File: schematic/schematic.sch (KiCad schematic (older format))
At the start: 12 parts, among them SW1 SW_DIP_x01, U1 Teensy3.2_outer_pins, U2 BALANCE_ALARM

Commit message: Basic robot working.
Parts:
- removed U1: Teensy3.2_outer_pins, symbol Teensy3.2_outer_pins
- added CSENSE1, CSENSE2: W4953-A-COLOR-SENSOR, symbol W4953-A-COLOR-SENSOR
- added SW2: SW_Push, symbol SW_Push
- added U1: Teensy3.5_outer_pins, symbol Teensy3.5_outer_pins
- R1: value 400k -> 470k
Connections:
- net 3V3: now also OLED1.~ (Vcc(2.8-5.5V)), CSENSE1.~ (SDA), CSENSE2.~ (SDA), U1.~ (TX5_SCL0'A14_33)
- net 5V: now also U1.~ (TX5_SCL0'A14_33); no longer OLED1.~ (Vcc(2.8-5.5V))
- net CAM_RX: now also U1.~ (TX5_SCL0'A14_33)
- net CAM_TX: now also U1.~ (TX5_SCL0'A14_33)
- net GND: now also CSENSE1.~ (SDA), CSENSE2.~ (SDA), U1.~ (TX5_SCL0'A14_33)
- net LEncoderA: now also U1.~ (TX5_SCL0'A14_33)
- net LEncoderB: now also U1.~ (TX5_SCL0'A14_33)
- net L_FWD: now also U1.~ (TX5_SCL0'A14_33)
- net L_REV: now also U1.~ (TX5_SCL0'A14_33)
- net OLED_CS: now also U1.~ (TX5_SCL0'A14_33)
- net OLED_DC: now also U1.~ (TX5_SCL0'A14_33)
- net OLED_MOSI: now also U1.~ (TX5_SCL0'A14_33)
- net OLED_RESET: now also U1.~ (TX5_SCL0'A14_33)
- net OLED_SCK: now also U1.~ (TX5_SCL0'A14_33)
- net REncoderA: now also U1.~ (TX5_SCL0'A14_33)
- net REncoderB: now also U1.~ (TX5_SCL0'A14_33)
- net R_FWD: now also U1.~ (TX5_SCL0'A14_33)
- net R_REV: now also U1.~ (TX5_SCL0'A14_33)
- net at R1.2, R2.1: now also U1.~ (TX5_SCL0'A14_33)
- new net: SW2.1, U1.~ (TX5_SCL0'A14_33)
- new net: SW2.2, U1.~ (TX5_SCL0'A14_33)
- new net SCL0: CSENSE1.~ (SDA), CSENSE2.~ (SDA), U1.~ (TX5_SCL0'A14_33)
- new net SDA0: CSENSE1.~ (SDA), CSENSE2.~ (SDA), U1.~ (TX5_SCL0'A14_33)
- no-connect marks 16 -> 8
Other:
- note removed: "<- future: gyro i2c, \n<- interrupt\n"
- note removed: "GND: Power ground\nVCC: 2.8-5.5V power supply\nD0: CLK clock\nD1: MOSI data\nRST: Reset\nDC: Data / command\nCS: Chip-select signal"
- moved on the sheet: CAM1, L_MTR1, MCC1, R_MTR1
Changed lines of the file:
@@
 encoding utf-8
 Sheet 1 1
-Title ""
+Title "Colored Line Following Robot"
 Date ""
-Rev ""
-Comp ""
-Comment1 ""
-Comment2 ""
-Comment3 ""
+Rev "0"
+Comp "Brian Erickson"
+Comment1 "comment 1"
+Comment2 "comment 2"
+Comment3 "comment 3"
 Comment4 ""
 $EndDescr
-Text GLabel 7000 4250 0    60   Input ~ 0
+Text GLabel 6250 4500 0    60   Input ~ 0
 LMotor-
-Text GLabel 7000 4750 0    60   Input ~ 0
+Text GLabel 6250 5000 0    60   Input ~ 0
 LMotor+
-Text GLabel 7000 4350 0    60   Input ~ 0
-GND
-Text GLabel 7000 4450 0    60   Input ~ 0
-3V3
-Text GLabel 7000 4550 0    60   Input ~ 0
+Text GLabel 6250 4600 0    60   Input ~ 0
+GND
+Text GLabel 6250 4700 0    60   Input ~ 0
+3V3
+Text GLabel 6250 4800 0    60   Input ~ 0
 LEncoderA
-Text GLabel 7000 4650 0    60   Input ~ 0
+Text GLabel 6250 4900 0    60   Input ~ 0
 LEncoderB
-Text GLabel 8650 4250 0    60   Input ~ 0
+Text GLabel 7900 4500 0    60   Input ~ 0
 RMotor-
-Text GLabel 8650 4750 0    60   Input ~ 0
+Text GLabel 7900 5000 0    60   Input ~ 0
 LMotor+
-Text GLabel 8650 4350 0    60   Input ~ 0
-GND
-Text GLabel 8650 4450 0    60   Input ~ 0
-3V3
-Text GLabel 8650 4550 0    60   Input ~ 0
+Text GLabel 7900 4600 0    60   Input ~ 0
+GND
+Text GLabel 7900 4700 0    60   Input ~ 0
+3V3
+Text GLabel 7900 4800 0    60   Input ~ 0
 REncoderA
-Text GLabel 8650 4650 0    60   Input ~ 0
+Text GLabel 7900 4900 0    60   Input ~ 0
 REncoderB
 Text GLabel 2500 6100 1    60   Input ~ 0
 GND
 Text GLabel 2600 6100 1    60   Input ~ 0
-5V
+3V3
 Text GLabel 2700 6100 1    60   Input ~ 0
 OLED_SCK
@@
 Text GLabel 9250 3550 0    60   Input ~ 0
 BAT-
-$Comp
-L Teensy3.2_outer_pins U1
-U 1 1 5A4FD2BC
-P 4950 2300
-F 0 "U1" H 4950 3100 60  0000 C CNN
-F 1 "Teensy3.2_outer_pins" H 4950 1350 60  0000 C CNN
-F 2 "" H 4950 2300 60  0000 C CNN
-F 3 "" H 4950 2300 60  0000 C CNN
-	1    4950 2300
-	1    0    0    -1
-$EndComp
-Text GLabel 3950 1700 0    60   Input ~ 0
+Text GLabel 3300 1700 0    60   Input ~ 0
 GND
 Text GLabel 5950 1700 2    60   Input ~ 0
@@
 L ENCODER_MOTOR L_MTR1
 U 1 1 5A4FD5AE
-P 7350 4450
-F 0 "L_MTR1" H 7350 4800 60  0000 C CNN
-F 1 "ENCODER_MOTOR" H 7400 4000 60  0000 C CNN
-F 2 "" H 7300 4050 60  0001 C CNN
-F 3 "" H 7300 4050 60  0001 C CNN
-	1    7350 4450
+P 6600 4700
+F 0 "L_MTR1" H 6600 5050 60  0000 C CNN
+F 1 "ENCODER_MOTOR" H 6650 4250 60  0000 C CNN
+F 2 "" H 6550 4300 60  0001 C CNN
+F 3 "" H 6550 4300 60  0001 C CNN
+	1    6600 4700
 	1    0    0    -1
 $EndComp
@@
 L ENCODER_MOTOR R_MTR1
 U 1 1 5A4FD6E6
-P 9000 4450
-F 0 "R_MTR1" H 9000 4800 60  0000 C CNN
-F 1 "ENCODER_MOTOR" H 9050 4000 60  0000 C CNN
-F 2 "" H 8950 4050 60  0001 C CNN
-F 3 "" H 8950 4050 60  0001 C CNN
-	1    9000 4450
+P 8250 4700
+F 0 "R_MTR1" H 8250 5050 60  0000 C CNN
+F 1 "ENCODER_MOTOR" H 8300 4250 60  0000 C CNN
+F 2 "" H 8200 4300 60  0001 C CNN
+F 3 "" H 8200 4300 60  0001 C CNN
+	1    8250 4700
 	1    0    0    -1
 $EndComp
@@
 $EndComp
 Text GLabel 5950 3000 2    60   Input ~ 0
-OLED_CLK
-Text GLabel 3950 2900 0    60   Input ~ 0
+OLED_SCK
+Text GLabel 3300 2900 0    60   Input ~ 0
 OLED_MOSI
-Text GLabel 3950 2800 0    60   Input ~ 0
+Text GLabel 3300 2800 0    60   Input ~ 0
 OLED_CS
-Text GLabel 3950 2600 0    60   Input ~ 0
+Text GLabel 3300 3000 0    60   Input ~ 0
 OLED_DC
-Text GLabel 3950 2700 0    60   Input ~ 0
+Text GLabel 3300 2700 0    60   Input ~ 0
 OLED_RESET
 $Comp
 L JEVOIS CAM1
 U 1 1 5A4FDEE7
-P 2250 2100
-F 0 "CAM1" H 2250 2450 60  0000 C CNN
-F 1 "JEVOIS" H 2250 1700 60  0000 C CNN
-F 2 "" H 2100 2200 60  0001 C CNN
-F 3 "" H 2100 2200 60  0001 C CNN
-	1    2250 2100
+P 7050 6050
+F 0 "CAM1" H 7050 6400 60  0000 C CNN
+F 1 "JEVOIS" H 7050 5650 60  0000 C CNN
+F 2 "" H 6900 6150 60  0001 C CNN
+F 3 "" H 6900 6150 60  0001 C CNN
+	1    7050 6050
 	-1   0    0    -1
 $EndComp
-Text GLabel 2900 2000 2    60   Input ~ 0
-GND
-Text GLabel 2900 1900 2    60   Input ~ 0
-3V3
-Text GLabel 1600 2200 0    60   Input ~ 0
+Text GLabel 7700 5950 2    60   Input ~ 0
+GND
+Text GLabel 7700 5850 2    60   Input ~ 0
+3V3
+Text GLabel 6400 6150 0    60   Input ~ 0
 5V
-Text GLabel 1600 2300 0    60   Input ~ 0
-GND
-Text GLabel 2900 2200 2    60   Input ~ 0
+Text GLabel 6400 6250 0    60   Input ~ 0
+GND
+Text GLabel 7700 6150 2    60   Input ~ 0
 CAM_TX
-Text GLabel 2900 2100 2    60   Input ~ 0
+Text GLabel 7700 6050 2    60   Input ~ 0
 CAM_RX
-Text GLabel 3950 1800 0    60   Input ~ 0
+Text GLabel 3300 1800 0    60   Input ~ 0
 CAM_TX
-Text GLabel 3950 1900 0    60   Input ~ 0
+Text GLabel 3300 1900 0    60   Input ~ 0
 CAM_RX
 $Comp
 L MOTOR_CONTROLLER_WANGDD22 MCC1
 U 1 1 5A4FE9B8
-P 2750 3750
-F 0 "MCC1" H 2750 4300 60  0000 C CNN
-F 1 "MOTOR_CONTROLLER_WANGDD22" H 2750 3250 60  0000 C CNN
-F 2 "" H 2500 3550 60  0001 C CNN
-F 3 "" H 2500 3550 60  0001 C CNN
-	1    2750 3750
-	1    0    0    -1
-$EndComp
-Text GLabel 2100 3650 0    60   Input ~ 0
+P 4600 6200
+F 0 "MCC1" H 4600 6750 60  0000 C CNN
+F 1 "MOTOR_CONTROLLER_WANGDD22" H 4600 5700 60  0000 C CNN
+F 2 "" H 4350 6000 60  0001 C CNN
+F 3 "" H 4350 6000 60  0001 C CNN
+	1    4600 6200
+	1    0    0    -1
+$EndComp
+Text GLabel 3950 6100 0    60   Input ~ 0
 L_FWD
-Text GLabel 2100 3750 0    60   Input ~ 0
+Text GLabel 3950 6200 0    60   Input ~ 0
 L_REV
-Text GLabel 2100 3900 0    60   Input ~ 0
+Text GLabel 3950 6350 0    60   Input ~ 0
 R_FWD
-Text GLabel 2100 4000 0    60   Input ~ 0
+Text GLabel 3950 6450 0    60   Input ~ 0
 R_REV
-Text GLabel 3500 3650 2    60   Input ~ 0
+Text GLabel 5350 6100 2    60   Input ~ 0
 LMotor-
-Text GLabel 3500 3550 2    60   Input ~ 0
+Text GLabel 5350 6000 2    60   Input ~ 0
 LMotor+
-Text GLabel 3500 3900 2    60   Input ~ 0
+Text GLabel 5350 6350 2    60   Input ~ 0
 RMotor-
-Text GLabel 3500 3800 2    60   Input ~ 0
+Text GLabel 5350 6250 2    60   Input ~ 0
 LMotor+
-Text GLabel 2100 3400 0    60   Input ~ 0
+Text GLabel 3950 5850 0    60   Input ~ 0
 BAT+
-Text GLabel 2100 3500 0    60   Input ~ 0
+Text GLabel 3950 5950 0    60   Input ~ 0
 BAT-
-Text GLabel 3950 2300 0    60   Input ~ 0
+Text GLabel 3300 2300 0    60   Input ~ 0
 L_FWD
-Text GLabel 3950 2400 0    60   Input ~ 0
+Text GLabel 3300 2400 0    60   Input ~ 0
 L_REV
 Text GLabel 5950 2100 2    60   Input ~ 0
@@
 Text GLabel 5950 2200 2    60   Input ~ 0
 R_REV
-Text GLabel 5950 2600 2    60   Input ~ 0
+Text GLabel 5950 2800 2    60   Input ~ 0
 LEncoderA
-Text GLabel 5950 2700 2    60   Input ~ 0
+Text GLabel 5950 2900 2    60   Input ~ 0
 LEncoderB
-Text GLabel 5950 2800 2    60   Input ~ 0
+Text GLabel 3300 2500 0    60   Input ~ 0
 REncoderA
-Text GLabel 5950 2900 2    60   Input ~ 0
+Text GLabel 3300 2600 0    60   Input ~ 0
 REncoderB
 NoConn ~ 5950 1800
@@
 NoConn ~ 9150 1800
 NoConn ~ 9050 1800
-NoConn ~ 3950 2000
-NoConn ~ 3950 2100
-NoConn ~ 3950 2200
-NoConn ~ 3950 2500
-NoConn ~ 3950 3000
 $Comp
 L SW_DIP_x01 SW1
@@
 P 7450 1850
 F 0 "R1" V 7530 1850 50  0000 C CNN
-F 1 "400k" V 7450 1850 50  0000 C CNN
+F 1 "470k" V 7450 1850 50  0000 C CNN
 F 2 "" V 7380 1850 50  0001 C CNN
 F 3 "" H 7450 1850 50  0001 C CNN
@@
 $EndComp
 $Comp
-L GND #PWR01
+L GND #PWR1
 U 1 1 5A511792
 P 7450 2350
-F 0 "#PWR01" H 7450 2100 50  0001 C CNN
+F 0 "#PWR1" H 7450 2100 50  0001 C CNN
 F 1 "GND" H 7450 2200 50  0000 C CNN
 F 2 "" H 7450 2350 50  0001 C CNN
@@
 Connection ~ 7450 1550
 Connection ~ 7450 950
-Text Notes 6050 2450 0    60   ~ 0
-<- future: gyro i2c, \n<- interrupt\n
-NoConn ~ 5950 2400
-NoConn ~ 5950 2500
-NoConn ~ 5950 2300
-$Comp
-L PWR_FLAG #FLG02
+$Comp
+L PWR_FLAG #FLG1
 U 1 1 5A51263B
 P 7700 950
-F 0 "#FLG02" H 7700 1025 50  0001 C CNN
+F 0 "#FLG1" H 7700 1025 50  0001 C CNN
 F 1 "PWR_FLAG" H 7700 1100 50  0000 C CNN
 F 2 "" H 7700 950 50  0001 C CNN
@@
 	1    0    0    -1
 $EndComp
-Text Notes 1100 5950 0    60   ~ 0
-GND: Power ground\nVCC: 2.8-5.5V power supply\nD0: CLK clock\nD1: MOSI data\nRST: Reset\nDC: Data / command\nCS: Chip-select signal
+$Comp
+L W4953-A-COLOR-SENSOR CSENSE1
+U 1 1 5A58EBFA
+P 9300 4700
+F 0 "CSENSE1" H 9250 5050 60  0000 C CNN
+F 1 "W4953-A-COLOR-SENSOR" H 9300 4350 60  0000 C CNN
+F 2 "" H 9200 4500 60  0001 C CNN
+F 3 "" H 9200 4500 60  0001 C CNN
+	1    9300 4700
+	1    0    0    -1
+$EndComp
+$Comp
+L W4953-A-COLOR-SENSOR CSENSE2
+U 1 1 5A58EC49
+P 9300 5650
+F 0 "CSENSE2" H 9250 6000 60  0000 C CNN
+F 1 "W4953-A-COLOR-SENSOR" H 9300 5300 60  0000 C CNN
+F 2 "" H 9200 5450 60  0001 C CNN
+F 3 "" H 9200 5450 60  0001 C CNN
+	1    9300 5650
+	1    0    0    -1
+$EndComp
+Text GLabel 9000 5500 0    60   Input ~ 0
+GND
+Text GLabel 9000 5600 0    60   Input ~ 0
+3V3
+Text GLabel 9000 5700 0    60   Input ~ 0
+SCL0
+Text GLabel 9000 5800 0    60   Input ~ 0
+SDA0
+Text GLabel 5950 2400 2    60   Input ~ 0
+SCL0
+Text GLabel 5950 2500 2    60   Input ~ 0
+SDA0
+Text GLabel 9000 4550 0    60   Input ~ 0
+GND
+Text GLabel 9000 4650 0    60   Input ~ 0
+3V3
+Text GLabel 9000 4750 0    60   Input ~ 0
+SCL0
+Text GLabel 9000 4850 0    60   Input ~ 0
+SDA0
+$Comp
+L Teensy3.5_outer_pins U1
+U 1 1 5A590923
+P 4600 3050
+F 0 "U1" H 4600 4600 60  0000 C CNN
+F 1 "Teensy3.5_outer_pins" H 4600 1900 60  0000 C CNN
+F 2 "" H 4600 3800 60  0000 C CNN
+F 3 "" H 4600 3800 60  0000 C CNN
+	1    4600 3050
+	1    0    0    -1
+$EndComp
+$Comp
+L SW_Push SW2
+U 1 1 5A5D70A9
+P 2800 3800
+F 0 "SW2" H 2850 3900 50  0000 L CNN
+F 1 "SW_Push" H 2800 3740 50  0000 C CNN
+F 2 "" H 2800 4000 50  0001 C CNN
+F 3 "" H 2800 4000 50  0001 C CNN
+	1    2800 3800
+	1    0    0    -1
+$EndComp
+Wire Wire Line
+	2600 3800 2600 4000
+Wire Wire Line
+	2600 4000 3300 4000
+Wire Wire Line
+	3300 3800 3000 3800
 $EndSCHEMATC

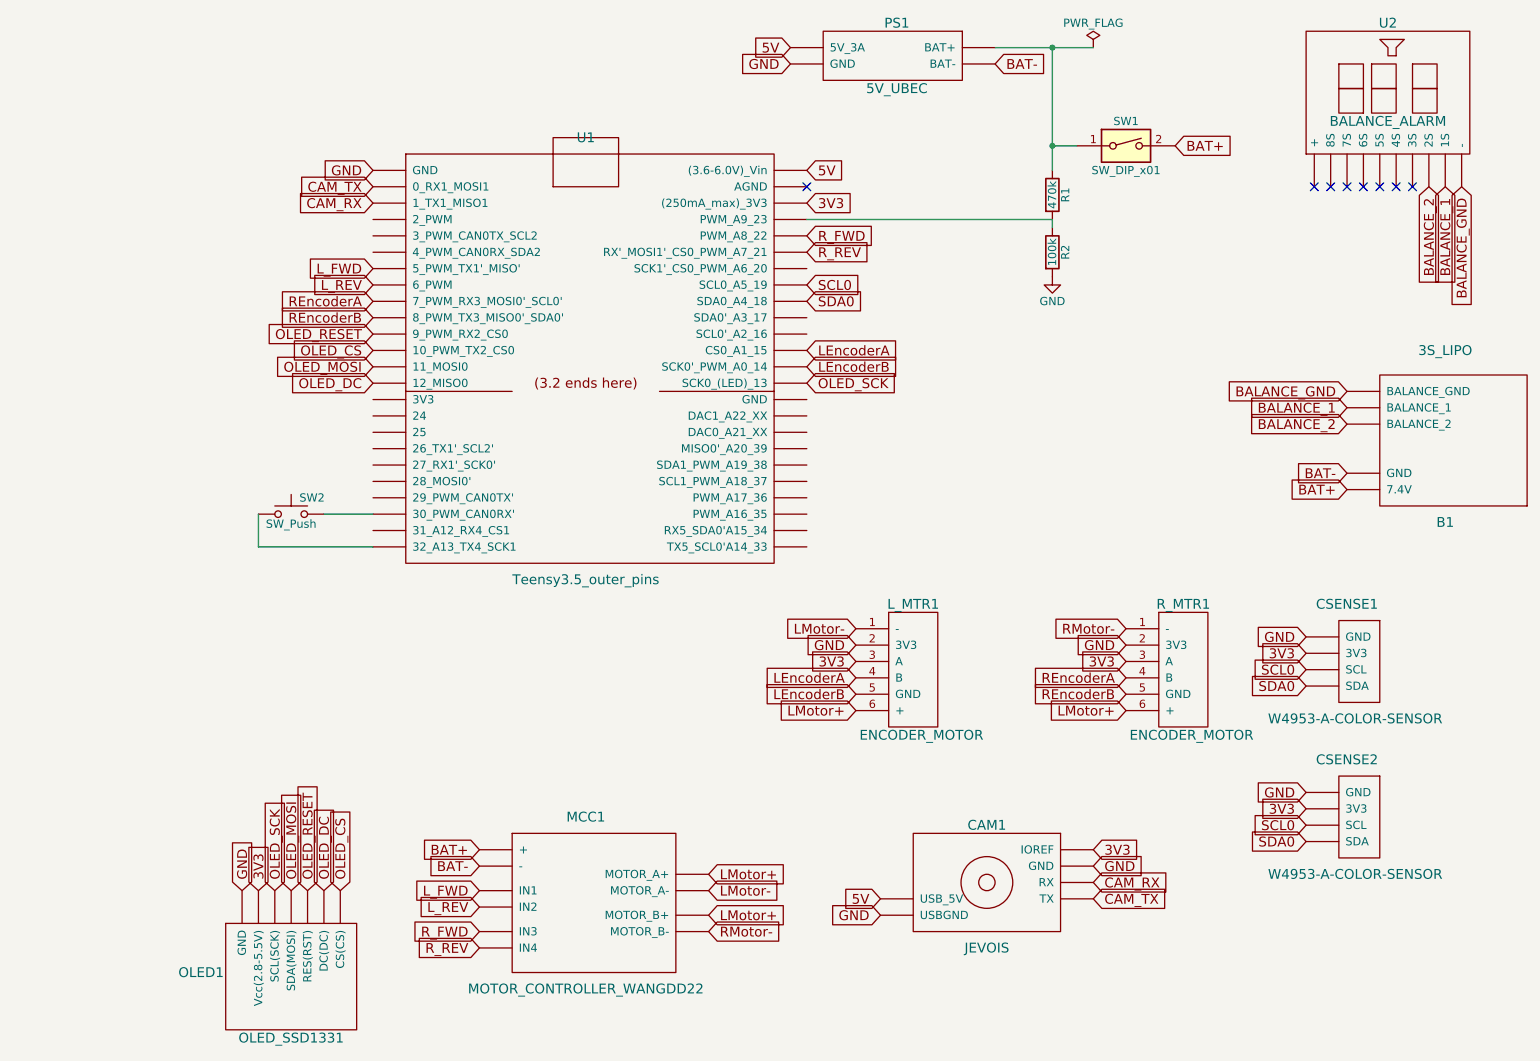
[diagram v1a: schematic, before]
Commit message: Added bluetooth, fixed motors.
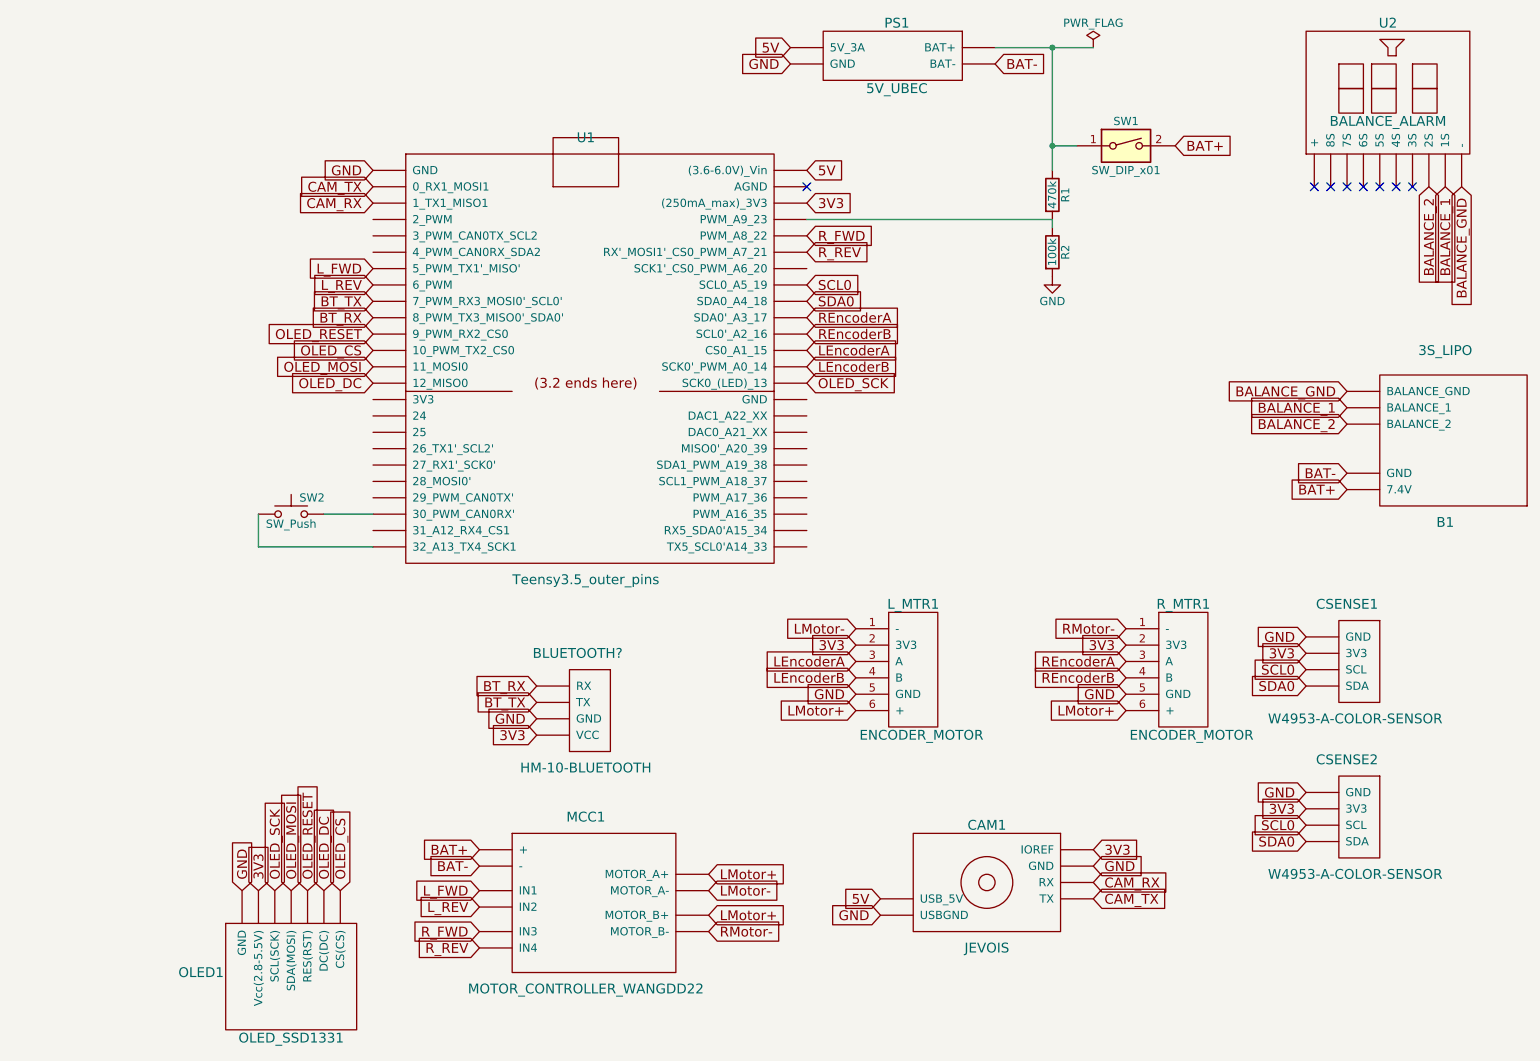
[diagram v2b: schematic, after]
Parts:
- added BLUETOOTH?: HM-10-BLUETOOTH, symbol HM-10-BLUETOOTH
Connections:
- net 3V3: now also L_MTR1.2 (3V3), R_MTR1.2 (3V3), BLUETOOTH?.~ (VCC); no longer L_MTR1.3 (A), R_MTR1.3 (A)
- net GND: now also L_MTR1.5 (GND), R_MTR1.5 (GND), BLUETOOTH?.~ (VCC); no longer L_MTR1.2 (3V3), R_MTR1.2 (3V3)
- net LEncoderA: now also L_MTR1.3 (A); no longer L_MTR1.4 (B)
- net LEncoderB: now also L_MTR1.4 (B); no longer L_MTR1.5 (GND)
- net REncoderA: now also R_MTR1.3 (A); no longer R_MTR1.4 (B)
- net REncoderB: now also R_MTR1.4 (B); no longer R_MTR1.5 (GND)
- new net BT_RX: BLUETOOTH?.~ (VCC), U1.~ (TX5_SCL0'A14_33)
- new net BT_TX: BLUETOOTH?.~ (VCC), U1.~ (TX5_SCL0'A14_33)
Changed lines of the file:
@@
 Rev "0"
 Comp "Brian Erickson"
-Comment1 "comment 1"
-Comment2 "comment 2"
-Comment3 "comment 3"
+Comment1 ""
+Comment2 ""
+Comment3 ""
 Comment4 ""
 $EndDescr
@@
 Text GLabel 6250 5000 0    60   Input ~ 0
 LMotor+
+Text GLabel 6250 4900 0    60   Input ~ 0
+GND
 Text GLabel 6250 4600 0    60   Input ~ 0
-GND
+3V3
 Text GLabel 6250 4700 0    60   Input ~ 0
-3V3
+LEncoderA
 Text GLabel 6250 4800 0    60   Input ~ 0
-LEncoderA
-Text GLabel 6250 4900 0    60   Input ~ 0
 LEncoderB
 Text GLabel 7900 4500 0    60   Input ~ 0
@@
 Text GLabel 7900 5000 0    60   Input ~ 0
 LMotor+
+Text GLabel 7900 4900 0    60   Input ~ 0
+GND
 Text GLabel 7900 4600 0    60   Input ~ 0
-GND
+3V3
 Text GLabel 7900 4700 0    60   Input ~ 0
-3V3
+REncoderA
 Text GLabel 7900 4800 0    60   Input ~ 0
-REncoderA
-Text GLabel 7900 4900 0    60   Input ~ 0
 REncoderB
 Text GLabel 2500 6100 1    60   Input ~ 0
@@
 Text GLabel 5950 2900 2    60   Input ~ 0
 LEncoderB
-Text GLabel 3300 2500 0    60   Input ~ 0
+Text GLabel 5950 2600 2    60   Input ~ 0
 REncoderA
-Text GLabel 3300 2600 0    60   Input ~ 0
+Text GLabel 5950 2700 2    60   Input ~ 0
 REncoderB
 NoConn ~ 5950 1800
@@
 Wire Wire Line
 	3300 3800 3000 3800
+Text GLabel 3300 2500 0    60   Input ~ 0
+BT_TX
+Text GLabel 3300 2600 0    60   Input ~ 0
+BT_RX
+$Comp
+L HM-10-BLUETOOTH BLUETOOTH?
+U 1 1 5A6C158D
+P 4600 5000
+F 0 "BLUETOOTH?" H 4550 5350 60  0000 C CNN
+F 1 "HM-10-BLUETOOTH" H 4600 4650 60  0000 C CNN
+F 2 "" H 4500 4800 60  0001 C CNN
+F 3 "" H 4500 4800 60  0001 C CNN
+	1    4600 5000
+	1    0    0    -1
+$EndComp
+Text GLabel 4300 4950 0    60   Input ~ 0
+BT_TX
+Text GLabel 4300 4850 0    60   Input ~ 0
+BT_RX
+Text GLabel 4300 5150 0    60   Input ~ 0
+3V3
+Text GLabel 4300 5050 0    60   Input ~ 0
+GND
 $EndSCHEMATC

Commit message: resistors
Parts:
- R1: value 470k -> 463.1k
- R2: value 100k -> 98.28k
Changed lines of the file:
@@
 P 7450 1850
 F 0 "R1" V 7530 1850 50  0000 C CNN
-F 1 "470k" V 7450 1850 50  0000 C CNN
+F 1 "463.1k" V 7450 1850 50  0000 C CNN
 F 2 "" V 7380 1850 50  0001 C CNN
 F 3 "" H 7450 1850 50  0001 C CNN
@@
 P 7450 2200
 F 0 "R2" V 7530 2200 50  0000 C CNN
-F 1 "100k" V 7450 2200 50  0000 C CNN
+F 1 "98.28k" V 7450 2200 50  0000 C CNN
 F 2 "" V 7380 2200 50  0001 C CNN
 F 3 "" H 7450 2200 50  0001 C CNN
